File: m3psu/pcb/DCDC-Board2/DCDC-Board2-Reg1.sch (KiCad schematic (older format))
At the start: 38 parts

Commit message: Start DC/DC routing
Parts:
- removed R?: 10k, agg:0402, symbol R
- gave numbers to parts that had none: 35
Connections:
- net at IC1.14 (RUN0), R2.2: now also IC1.15 (RUN1)

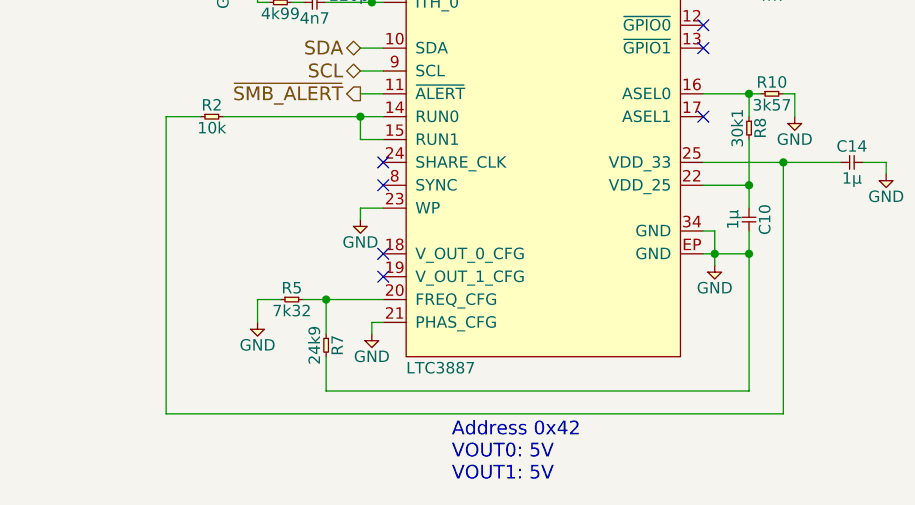
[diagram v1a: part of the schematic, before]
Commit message: Finish routing DC-DC Board 2
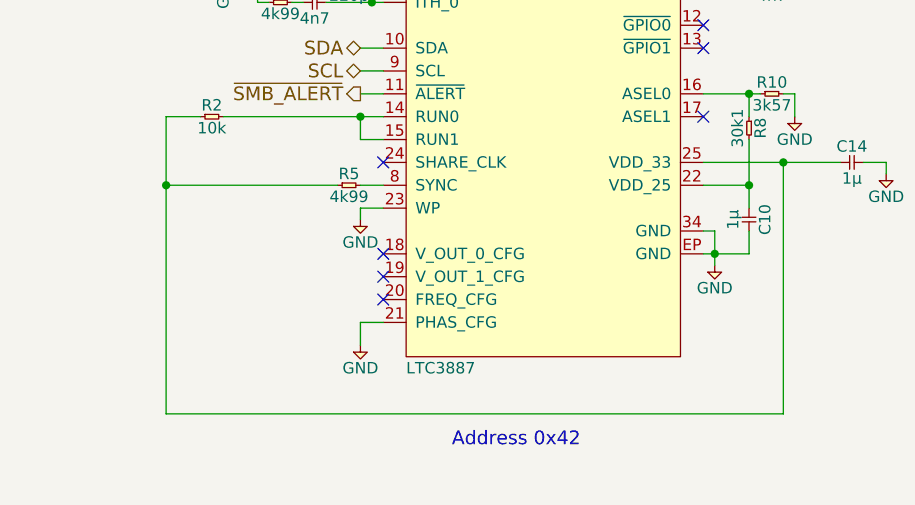
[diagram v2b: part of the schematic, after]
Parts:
- removed R7: 24k9, agg:0402, symbol R
- R5: value 7k32 -> 4k99; Farnell 2073231 -> 1469715
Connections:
- net GND: no longer R5.1
- net at IC1.20 (FREQ_CFG): no longer R5.2
- net at C14.1, IC1.25 (VDD_33), R2.1: now also R5.1
- net at IC1.8 (SYNC): now also R5.2
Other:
- note added: "Address 0x42"
- note removed: "Address 0x42\nVOUT0: 5V\nVOUT1: 5V"
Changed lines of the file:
@@
 EESchema Schematic File Version 2
 LIBS:agg-kicad
+LIBS:DCDC-Board2-cache
 EELAYER 25 0
 EELAYER END
@@
 $EndComp
 NoConn ~ 5100 4550
-NoConn ~ 5100 4650
 NoConn ~ 6500 4350
 $Comp
@@
 	0    1    1    0
 $EndComp
-$Comp
-L GND #PWR038
-U 1 1 56D56F19
-P 5050 5300
-F 0 "#PWR038" H 4920 5340 50  0001 L CNN
-F 1 "GND" H 5050 5200 50  0000 C CNN
-F 2 "" H 5050 5300 60  0000 C CNN
-F 3 "" H 5050 5300 60  0000 C CNN
-	1    5050 5300
-	1    0    0    -1
-$EndComp
-Wire Wire Line
-	5050 5250 5050 5300
 Wire Wire Line
 	7050 3700 7100 3700
@@
 	5000 4750 5000 4800
 Wire Wire Line
-	5050 5250 5100 5250
-Connection ~ 6700 4950
-Wire Wire Line
 	7200 4550 7300 4550
 Wire Wire Line
@@
 Wire Wire Line
 	5000 3550 5100 3550
-Wire Wire Line
-	6700 4850 6700 5550
 Wire Wire Line
 	6500 4550 7100 4550
@@
 Connection ~ 5050 3550
 $Comp
-L GND #PWR039
+L GND #PWR038
 U 1 1 56D56FBE
 P 6750 3550
-F 0 "#PWR039" H 6620 3590 50  0001 L CNN
+F 0 "#PWR038" H 6620 3590 50  0001 L CNN
 F 1 "GND" H 6750 3450 50  0000 C CNN
 F 2 "" H 6750 3550 60  0000 C CNN
@@
 Text HLabel 5000 4250 0    60   Output ~ 0
 ~SMB_ALERT
-Text Notes 5400 5950 0    60   ~ 0
-Address 0x42\nVOUT0: 5V\nVOUT1: 5V
+Text Notes 5400 5800 0    60   ~ 0
+Address 0x42
 Wire Wire Line
 	5000 4750 5100 4750
-$Comp
-L R R7
-U 1 1 56DDC75E
-P 4850 5300
-F 0 "R7" H 4900 5350 50  0000 C CNN
-F 1 "24k9" H 4900 5250 50  0000 C CNN
-F 2 "agg:0402" H 4850 5300 50  0001 C CNN
-F 3 "" H 4850 5300 50  0001 C CNN
-F 4 "1803690" H 4850 5300 60  0001 C CNN "Farnell"
-	1    4850 5300
-	0    1    1    0
-$EndComp
-$Comp
-L GND #PWR040
-U 1 1 56DDC765
-P 4550 5250
-F 0 "#PWR040" H 4420 5290 50  0001 L CNN
-F 1 "GND" H 4550 5150 50  0000 C CNN
-F 2 "" H 4550 5250 60  0000 C CNN
-F 3 "" H 4550 5250 60  0000 C CNN
-	1    4550 5250
-	1    0    0    -1
-$EndComp
-Connection ~ 4850 5150
-Wire Wire Line
-	4750 5150 5100 5150
-Wire Wire Line
-	4850 5150 4850 5300
-Wire Wire Line
-	4850 5400 4850 5550
-$Comp
-L R R5
-U 1 1 56DDC770
-P 4650 5150
-F 0 "R5" H 4700 5200 50  0000 C CNN
-F 1 "7k32" H 4700 5100 50  0000 C CNN
-F 2 "agg:0402" H 4650 5150 50  0001 C CNN
-F 3 "" H 4650 5150 50  0001 C CNN
-F 4 "2073231" H 4650 5150 60  0001 C CNN "Farnell"
-	1    4650 5150
-	1    0    0    -1
-$EndComp
-Wire Wire Line
-	4650 5150 4550 5150
-Wire Wire Line
-	4550 5150 4550 5250
-Wire Wire Line
-	4850 5550 6700 5550
 Wire Wire Line
 	4150 5650 6850 5650
@@
 	5000 4450 5000 4350
 Connection ~ 5000 4350
+Wire Wire Line
+	6700 4950 6700 4850
+NoConn ~ 5100 5150
+$Comp
+L R R5
+U 1 1 571930DA
+P 4900 4650
+F 0 "R5" H 4950 4700 50  0000 C CNN
+F 1 "4k99" H 4950 4600 50  0000 C CNN
+F 2 "agg:0402" H 4900 4650 50  0001 C CNN
+F 3 "" H 4900 4650 50  0001 C CNN
+F 4 "1469715" H 4900 4650 60  0001 C CNN "Farnell"
+	1    4900 4650
+	1    0    0    -1
+$EndComp
+Wire Wire Line
+	5100 4650 5000 4650
+$Comp
+L GND #PWR039
+U 1 1 57193348
+P 5000 5350
+F 0 "#PWR039" H 4870 5390 50  0001 L CNN
+F 1 "GND" H 5000 5250 50  0000 C CNN
+F 2 "" H 5000 5350 60  0000 C CNN
+F 3 "" H 5000 5350 60  0000 C CNN
+	1    5000 5350
+	1    0    0    -1
+$EndComp
+Wire Wire Line
+	5100 5250 5000 5250
+Wire Wire Line
+	5000 5250 5000 5350
+Wire Wire Line
+	4900 4650 4150 4650
+Connection ~ 4150 4650
 $EndSCHEMATC

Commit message: Fixed GPIO 1&2 pull to VDD33 with 10k. Fixed V_IN 100n decoupling cap. Fixed BOOST caps to 100n.
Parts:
- added C31: 100n, agg:0402, symbol C
- added R18: 10k, agg:0402, symbol R
- C11, C2: value 1n5 -> 100n; Farnell 2210833 -> 2496811
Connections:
- net GND: now also C31.2
- net VCC: now also C31.1
- net at IC1.12 (~GPIO0): now also IC1.13 (~GPIO1), R18.1
- net at C14.1, IC1.25 (VDD_33), R2.1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: now also R18.2
- no-connect marks 7 -> 5
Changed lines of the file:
@@
 P 6750 2850
 F 0 "C11" H 6800 2920 50  0000 C CNN
-F 1 "1n5" H 6800 2780 50  0000 C CNN
+F 1 "100n" H 6800 2780 50  0000 C CNN
 F 2 "agg:0402" H 6750 2850 50  0001 C CNN
 F 3 "" H 6750 2850 50  0001 C CNN
-F 4 "2210833" H 6750 2850 60  0001 C CNN "Farnell"
+F 4 "2496811" H 6750 2850 60  0001 C CNN "Farnell"
 	1    6750 2850
 	1    0    0    -1
@@
 P 4750 2850
 F 0 "C2" H 4800 2920 50  0000 C CNN
-F 1 "1n5" H 4800 2780 50  0000 C CNN
+F 1 "100n" H 4800 2780 50  0000 C CNN
 F 2 "agg:0402" H 4750 2850 50  0001 C CNN
 F 3 "" H 4750 2850 50  0001 C CNN
-F 4 "2210833" H 4750 2850 60  0001 C CNN "Farnell"
+F 4 "2496811" H 4750 2850 60  0001 C CNN "Farnell"
 	1    4750 2850
 	1    0    0    -1
@@
 Wire Wire Line
 	6500 3550 6750 3550
-NoConn ~ 6500 3950
-NoConn ~ 6500 4050
 $Comp
 L C C9
@@
 	4900 4650 4150 4650
 Connection ~ 4150 4650
+$Comp
+L R R18
+U 1 1 57472437
+P 7000 4100
+F 0 "R18" H 7050 4150 50  0000 C CNN
+F 1 "10k" H 7050 4050 50  0000 C CNN
+F 2 "agg:0402" H 7000 4100 50  0001 C CNN
+F 3 "" H 7000 4100 50  0001 C CNN
+F 4 "2447096" H 7000 4100 60  0001 C CNN "Farnell"
+	1    7000 4100
+	0    1    1    0
+$EndComp
+Wire Wire Line
+	7000 4200 7000 4550
+Connection ~ 7000 4550
+Wire Wire Line
+	7000 4100 7000 4000
+Wire Wire Line
+	6500 3950 6550 3950
+Wire Wire Line
+	6550 3950 6550 4050
+Wire Wire Line
+	6550 4050 6500 4050
+Wire Wire Line
+	7000 4000 6550 4000
+Connection ~ 6550 4000
+$Comp
+L C C31
+U 1 1 574761D4
+P 5150 2200
+F 0 "C31" H 5200 2270 50  0000 C CNN
+F 1 "100n" H 5200 2130 50  0000 C CNN
+F 2 "agg:0402" H 5150 2200 50  0001 C CNN
+F 3 "" H 5150 2200 50  0001 C CNN
+F 4 "2496811" H 5150 2200 60  0001 C CNN "Farnell"
+	1    5150 2200
+	1    0    0    -1
+$EndComp
+Wire Wire Line
+	5150 2200 5100 2200
+Connection ~ 5100 2200
+$Comp
+L GND #PWR040
+U 1 1 57476564
+P 5350 2250
+F 0 "#PWR040" H 5220 2290 50  0001 L CNN
+F 1 "GND" H 5350 2150 50  0000 C CNN
+F 2 "" H 5350 2250 60  0000 C CNN
+F 3 "" H 5350 2250 60  0000 C CNN
+	1    5350 2250
+	1    0    0    -1
+$EndComp
+Wire Wire Line
+	5250 2200 5350 2200
+Wire Wire Line
+	5350 2200 5350 2250
 $EndSCHEMATC

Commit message: Added in ground pour on top side of DCDC board. DRC is not happy now...
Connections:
- net GND: no longer IC1.21 (PHAS_CFG)
- no-connect marks 5 -> 6
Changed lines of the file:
@@
 Wire Wire Line
 	5100 4650 5000 4650
-$Comp
-L GND #PWR039
-U 1 1 57193348
-P 5000 5350
-F 0 "#PWR039" H 4870 5390 50  0001 L CNN
-F 1 "GND" H 5000 5250 50  0000 C CNN
-F 2 "" H 5000 5350 60  0000 C CNN
-F 3 "" H 5000 5350 60  0000 C CNN
-	1    5000 5350
-	1    0    0    -1
-$EndComp
-Wire Wire Line
-	5100 5250 5000 5250
-Wire Wire Line
-	5000 5250 5000 5350
 Wire Wire Line
 	4900 4650 4150 4650
@@
 Connection ~ 5100 2200
 $Comp
-L GND #PWR040
+L GND #PWR039
 U 1 1 57476564
 P 5350 2250
-F 0 "#PWR040" H 5220 2290 50  0001 L CNN
+F 0 "#PWR039" H 5220 2290 50  0001 L CNN
 F 1 "GND" H 5350 2150 50  0000 C CNN
 F 2 "" H 5350 2250 60  0000 C CNN
@@
 Wire Wire Line
 	5350 2200 5350 2250
+NoConn ~ 5100 5250
 $EndSCHEMATC

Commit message: BOM for DCDC board 2 (inc swap 22u cap for in-stock)
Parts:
- C1, C15, C7: Farnell 1907510 -> 2346925
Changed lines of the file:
@@
 F 2 "agg:0805" H 5800 2100 50  0001 C CNN
 F 3 "" H 5800 2100 50  0001 C CNN
-F 4 "1907510" H 5800 2100 60  0001 C CNN "Farnell"
+F 4 "2346925" H 5800 2100 60  0001 C CNN "Farnell"
 	1    5800 2100
 	0    1    1    0
@@
 F 2 "agg:0805" H 7650 3000 50  0001 C CNN
 F 3 "" H 7650 3000 50  0001 C CNN
-F 4 "1907510" H 7650 3000 60  0001 C CNN "Farnell"
+F 4 "2346925" H 7650 3000 60  0001 C CNN "Farnell"
 	1    7650 3000
 	0    1    1    0
@@
 F 2 "agg:0805" H 3950 3000 50  0001 C CNN
 F 3 "" H 3950 3000 50  0001 C CNN
-F 4 "1907510" H 3950 3000 60  0001 C CNN "Farnell"
+F 4 "2346925" H 3950 3000 60  0001 C CNN "Farnell"
 	1    3950 3000
 	0    1    1    0

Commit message: routed one regulator
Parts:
- C4: footprint agg:0603 -> agg:0402; Farnell 2426959 -> 2346881
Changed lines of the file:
@@
 F 0 "C4" H 4850 2520 50  0000 C CNN
 F 1 "4µ7" H 4850 2380 50  0000 C CNN
-F 2 "agg:0603" H 4800 2450 50  0001 C CNN
+F 2 "agg:0402" H 4800 2450 50  0001 C CNN
 F 3 "" H 4800 2450 50  0001 C CNN
-F 4 "2426959" H 4800 2450 60  0001 C CNN "Farnell"
+F 4 "2346881" H 4800 2450 60  0001 C CNN "Farnell"
 	1    4800 2450
 	0    1    1    0

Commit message: create DCDC1/2/3 from prototype
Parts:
- R10: value 3k57 -> 5k76; Farnell 2302693 -> (none)
- R8: value 30k1 -> 24k9; Farnell 2072900 -> (none)
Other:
- note added: "Address 0x44"
- note removed: "Address 0x42"
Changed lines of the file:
@@
 P 6750 4250
 F 0 "R10" H 6800 4300 50  0000 C CNN
-F 1 "3k57" H 6800 4200 50  0000 C CNN
+F 1 "5k76" H 6800 4200 50  0000 C CNN
 F 2 "agg:0402" H 6750 4250 50  0001 C CNN
 F 3 "" H 6750 4250 50  0001 C CNN
-F 4 "2302693" H 6750 4250 60  0001 C CNN "Farnell"
 	1    6750 4250
 	1    0    0    -1
@@
 P 6700 4350
 F 0 "R8" H 6750 4400 50  0000 C CNN
-F 1 "30k1" H 6750 4300 50  0000 C CNN
+F 1 "24k9" H 6750 4300 50  0000 C CNN
 F 2 "agg:0402" H 6700 4350 50  0001 C CNN
 F 3 "" H 6700 4350 50  0001 C CNN
-F 4 "2072900" H 6700 4350 60  0001 C CNN "Farnell"
 	1    6700 4350
 	0    1    1    0
@@
 ~SMB_ALERT
 Text Notes 5400 5800 0    60   ~ 0
-Address 0x42
+Address 0x44
 Wire Wire Line
 	5000 4750 5100 4750
